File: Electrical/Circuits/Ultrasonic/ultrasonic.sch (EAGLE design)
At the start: 2 parts, among them U1 HC-SR04

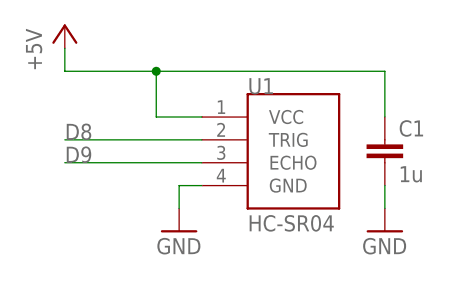
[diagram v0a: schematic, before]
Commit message: Updated Ultrasonic Schematic capacitance
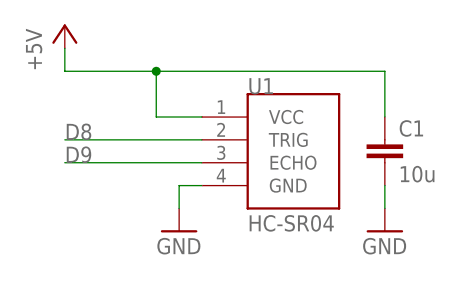
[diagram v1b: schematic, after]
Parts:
- C1: value 1u -> 10u
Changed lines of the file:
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@@
 <part name="FRAME1" library="IDP_library" deviceset="FRAME-A4L" device=""/>
 <part name="U1" library="IDP_library" deviceset="HC-SR04" device=""/>
-<part name="C1" library="IDP_library" deviceset="C-EU" device="075-032X103" package3d_urn="urn:adsk.eagle:package:23646/1" value="1u"/>
+<part name="C1" library="IDP_library" deviceset="C-EU" device="075-032X103" package3d_urn="urn:adsk.eagle:package:23646/1" value="10u"/>
 <part name="GND1" library="IDP_library" deviceset="GND" device=""/>
 <part name="P+1" library="IDP_library" deviceset="+5V" device=""/>
